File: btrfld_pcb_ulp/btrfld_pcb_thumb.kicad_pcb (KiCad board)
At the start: 2 copper layers, 53.7 x 30.8 mm, 13 parts

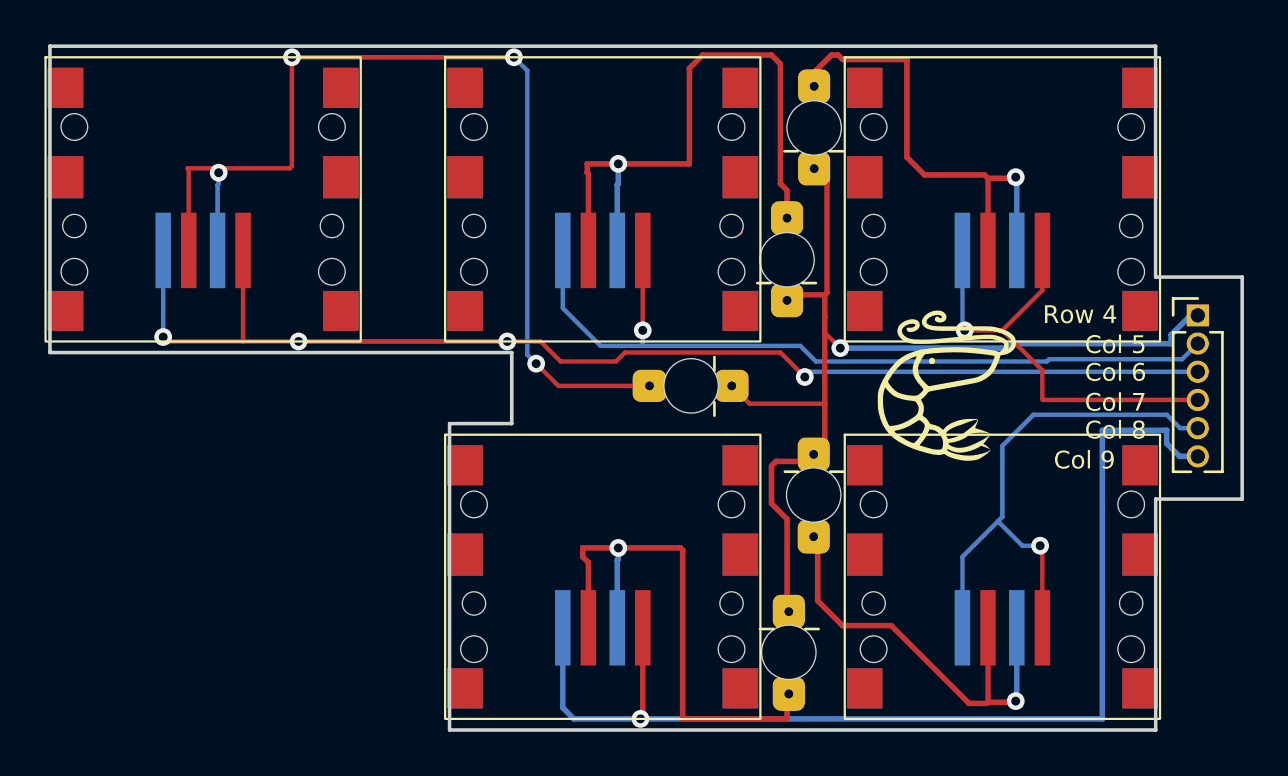
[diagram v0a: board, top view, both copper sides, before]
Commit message: added faster holes to pcb & cad thumb, reviewed traces
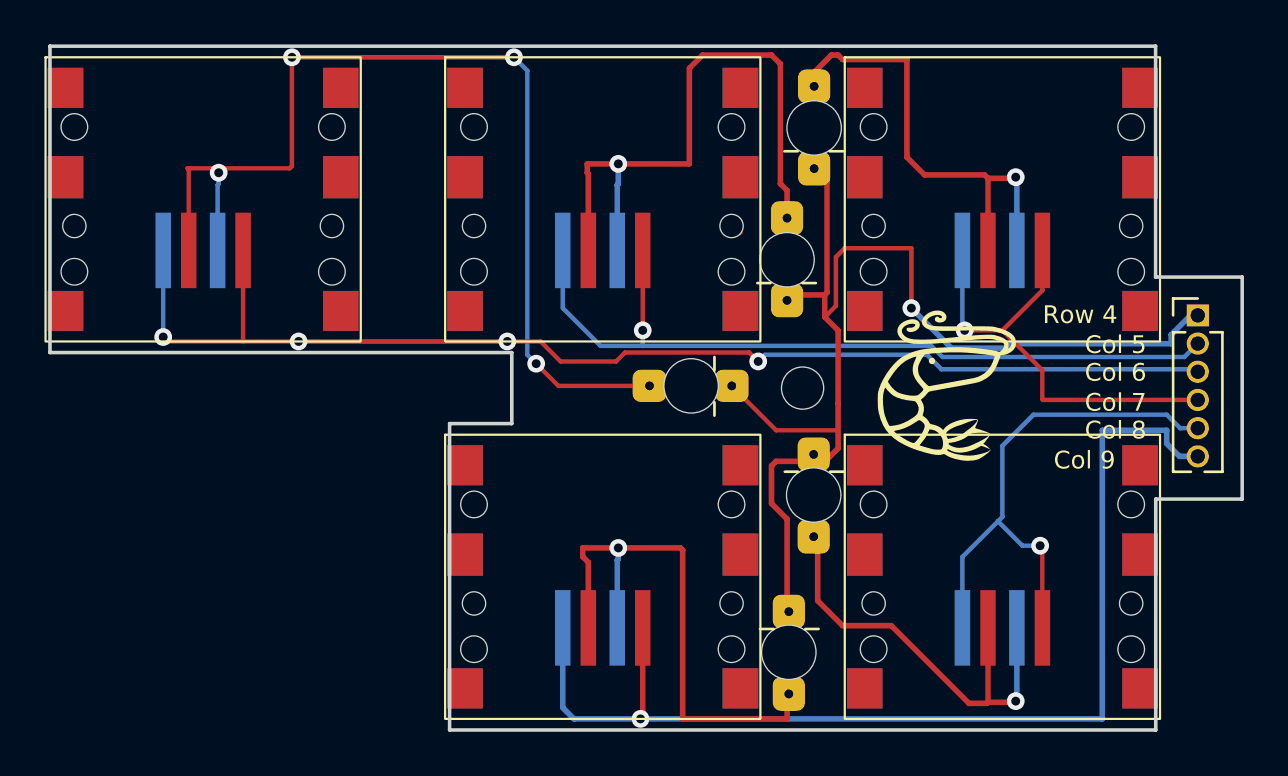
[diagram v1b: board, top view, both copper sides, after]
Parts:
- added ?: , , F.Cu at (149.1, 98.0)
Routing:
- net (no net): track 389.3 -> 397.0 mm
